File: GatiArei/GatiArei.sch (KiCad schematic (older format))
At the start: 38 parts

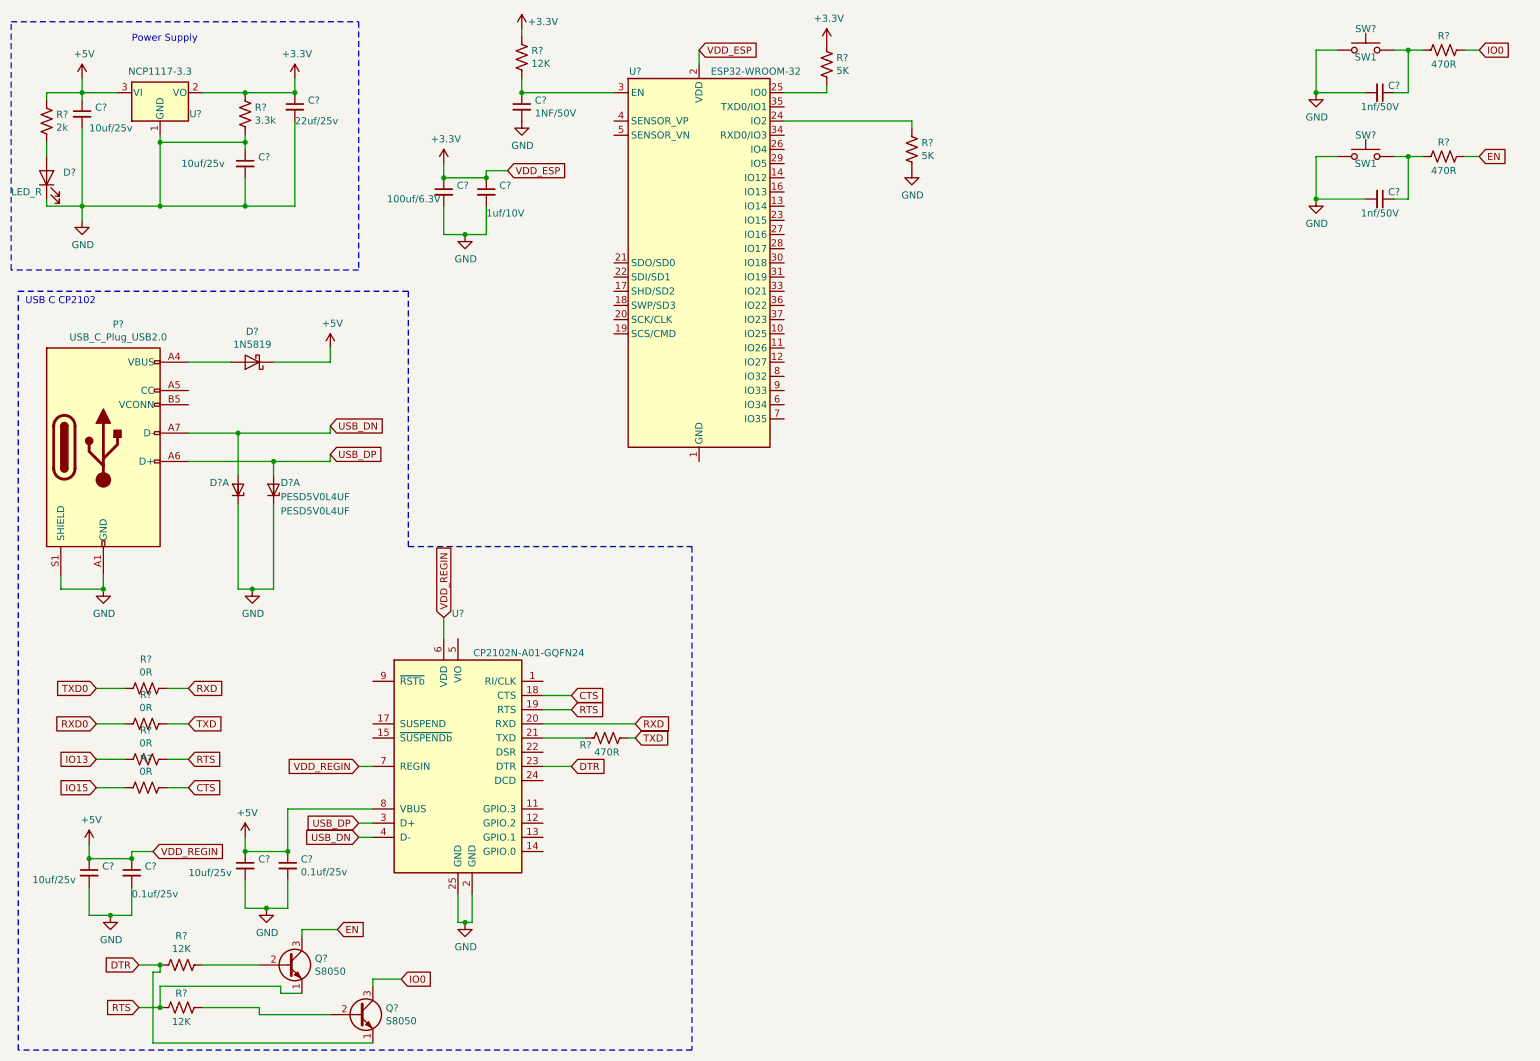
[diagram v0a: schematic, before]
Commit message: Adding the RFID and LCD port
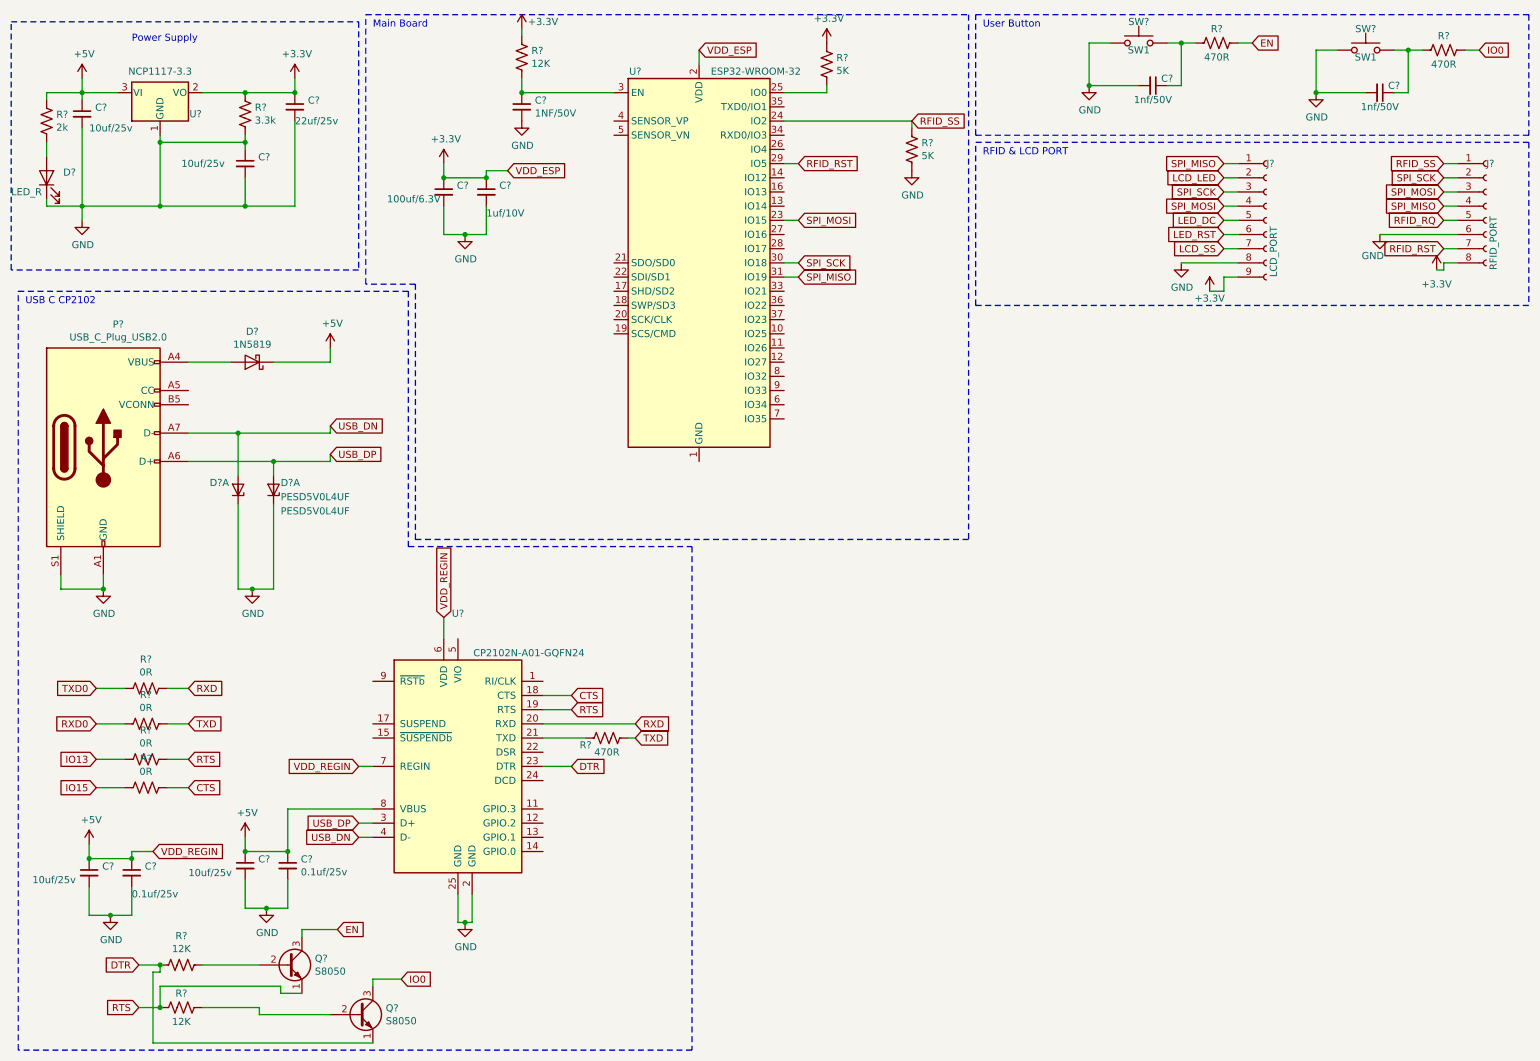
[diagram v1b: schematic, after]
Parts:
- added J?: RFID_PORT, symbol Connector:Conn_01x08_Female
- added J?: LCD_PORT, symbol Connector:Conn_01x09_Female
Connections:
- net +3V3: now also J?.8 (Pin_8), J?.9 (Pin_9)
- net GND: now also J?.6 (Pin_6), J?.8 (Pin_8)
- net SPI_MOSI: now reaches U?.23 (IO15)
- net SPI_MOSI: now also J?.3 (Pin_3), J?.4 (Pin_4)
- net RFID_SS: now reaches R?.1, U?.24 (IO2)
- net RFID_SS: now also J?.1 (Pin_1)
- net RFID_RST: now reaches U?.29 (IO5)
- net RFID_RST: now also J?.7 (Pin_7)
- net SPI_SCK: now reaches U?.30 (IO18)
- net SPI_SCK: now also J?.2 (Pin_2), J?.3 (Pin_3)
- net SPI_MISO: now reaches U?.31 (IO19)
- net SPI_MISO: now also J?.1 (Pin_1), J?.4 (Pin_4)
- new net LCD_LED: J?.2 (Pin_2)
- new net LCD_SS: J?.7 (Pin_7)
- new net LED_DC: J?.5 (Pin_5)
- new net LED_RST: J?.6 (Pin_6)
- new net RFID_RQ: J?.5 (Pin_5)
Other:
- note added: "Main Board"
- note added: "RFID & LCD PORT"
- note added: "User Button"
- moved on the sheet: C?, R?, SW?

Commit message: Adding Display Port
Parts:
- removed U?: NCP1117-3.3, Package_TO_SOT_SMD:SOT-223-3_TabPin2, symbol Regulator_Linear:NCP1117-3.3_SOT223
- added U1: MCP1700-3302E_SOT23, Package_TO_SOT_SMD:SOT-23, symbol Regulator_Linear:MCP1700-3302E_SOT23
- C1, C2, C4, C5: renamed from C?; footprint (none) -> Capacitor_SMD:C_1210_3225Metric
- C10, C11, C12, C3, C6, C7, C9: renamed from C?; footprint (none) -> Capacitor_SMD:C_0805_2012Metric
- C8: renamed from C?; footprint (none) -> Capacitor_Tantalum_SMD:CP_EIA-6032-15_Kemet-U
- D1: renamed from D?; footprint (none) -> LED_SMD:LED_0805_2012Metric
- J1: renamed from J?; footprint (none) -> Connector_PinHeader_2.54mm:PinHeader_1x09_P2.54mm_Vertical
- J2: renamed from J?; footprint (none) -> Connector_PinHeader_2.54mm:PinHeader_1x08_P2.54mm_Vertical
- P1: renamed from P?; footprint (none) -> Connector_USB:USB_C_Plug_Molex_105444
- R1, R10, R11, R12, R13, R14, R2, R3, R4, R5, R6, R7, R8, R9: renamed from R?; footprint (none) -> Resistor_SMD:R_0805_2012Metric
- SW1, SW2: renamed from SW?; footprint (none) -> Button_Switch_SMD:SW_DIP_SPSTx01_Slide_6.7x4.1mm_W6.73mm_P2.54mm_LowProfile_JPin
- gave numbers to parts that had none: 7
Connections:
- net LCD_LED is gone; now on net +3V3: J1.2 (Pin_2)
- net LED_DC is gone; now on net LCD_DC: J1.5 (Pin_5)
- net LED_RST is gone; now on net LCD_RST: J1.6 (Pin_6)
- net +3V3: now also U1.2 (VO)
- net +5V: now also U1.3 (VI)
- net GND: now also U1.1 (GND)
- net LCD_SS: now also U3.23 (IO15)
- net SPI_MOSI: now also U3.37 (IO23); no longer U3.23 (IO15)
- net LCD_DC: now reaches U3.16 (IO13)
- net LCD_RST: now reaches U3.26 (IO4)

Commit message: Adding PCB design
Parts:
- added J3: Bat_Con, Connector_PinHeader_2.00mm:PinHeader_1x02_P2.00mm_Vertical, symbol Connector:Conn_01x02_Female
- D2, D4: value PESD5V0L4UF -> ESD5V; footprint Package_TO_SOT_SMD:SOT-886 -> Package_TO_SOT_SMD:SOT-23
- D3: footprint Diode_THT:D_DO-41_SOD81_P10.16mm_Horizontal -> Diode_SMD:D_SMA
- P1: value USB_C_Plug_USB2.0 -> USB_C
- Q1, Q2: footprint Package_TO_SOT_THT:TO-92_Inline -> Package_TO_SOT_SMD:SOT-23
- U1: value MCP1700-3302E_SOT23 -> MCP1700
- U2: value CP2102N-A01-GQFN24 -> CP2102N
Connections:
- net +5V: now also J3.1 (Pin_1)
- net EN: now also C10.1, R9.2, U3.3 (EN)
- net GND: now also J3.2 (Pin_2)
- net IO0: now also R11.2, U3.25 (IO0)
- net RXD0: now also U3.34 (RXD0/IO3)
- net TXD0: now also U3.35 (TXD0/IO1)
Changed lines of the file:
@@
 P 3650 5800
 F 0 "U2" H 3650 6878 50  0000 C CNN
-F 1 "CP2102N-A01-GQFN24" H 4150 6600 50  0000 C CNN
+F 1 "CP2102N" H 4150 6600 50  0000 C CNN
 F 2 "Package_DFN_QFN:QFN-24-1EP_4x4mm_P0.5mm_EP2.6x2.6mm" H 4100 5000 50  0001 L CNN
 F 3 "http://www.silabs.com/support%20documents/technicaldocs/cp2102n-datasheet.pdf" H 3700 4750 50  0001 C CNN
@@
 P 1150 3550
 F 0 "P1" H 1255 4417 50  0000 C CNN
-F 1 "USB_C_Plug_USB2.0" H 1255 4326 50  0000 C CNN
+F 1 "USB_C" H 1255 4326 50  0000 C CNN
 F 2 "Connector_USB:USB_C_Plug_Molex_105444" H 1300 3550 50  0001 C CNN
 F 3 "https://www.usb.org/sites/default/files/documents/usb_type-c.zip" H 1300 3550 50  0001 C CNN
@@
 F 0 "D3" H 2200 2734 50  0000 C CNN
 F 1 "1N5819" H 2200 2825 50  0000 C CNN
-F 2 "Diode_THT:D_DO-41_SOD81_P10.16mm_Horizontal" H 2200 2775 50  0001 C CNN
+F 2 "Diode_SMD:D_SMA" H 2200 2775 50  0001 C CNN
 F 3 "http://www.vishay.com/docs/88525/1n5817.pdf" H 2200 2950 50  0001 C CNN
 	1    2200 2950
@@
 P 2100 3850
 F 0 "D2" V 2150 4050 50  0000 R CNN
-F 1 "PESD5V0L4UF" V 1950 3550 50  0000 R CNN
-F 2 "Package_TO_SOT_SMD:SOT-886" H 2100 3850 50  0001 C CNN
+F 1 "ESD5V" V 1950 3550 50  0000 R CNN
+F 2 "Package_TO_SOT_SMD:SOT-23" H 2100 3850 50  0001 C CNN
 F 3 "http://www.nxp.com/documents/data_sheet/PESDXL4UF_G_W.pdf" H 2100 3850 50  0001 C CNN
 	1    2100 3850
@@
 P 2350 3850
 F 0 "D4" V 2400 3800 50  0000 R CNN
-F 1 "PESD5V0L4UF" V 2300 3800 50  0000 R CNN
-F 2 "Package_TO_SOT_SMD:SOT-886" H 2350 3850 50  0001 C CNN
+F 1 "ESD5V" V 2300 3800 50  0000 R CNN
+F 2 "Package_TO_SOT_SMD:SOT-23" H 2350 3850 50  0001 C CNN
 F 3 "http://www.nxp.com/documents/data_sheet/PESDXL4UF_G_W.pdf" H 2350 3850 50  0001 C CNN
 	1    2350 3850
@@
 F 0 "Q1" H 2641 7246 50  0000 L CNN
 F 1 "S8050" H 2641 7155 50  0000 L CNN
-F 2 "Package_TO_SOT_THT:TO-92_Inline" H 2650 7125 50  0001 L CIN
+F 2 "Package_TO_SOT_SMD:SOT-23" H 2650 7125 50  0001 L CIN
 F 3 "http://www.unisonic.com.tw/datasheet/S8050.pdf" H 2450 7200 50  0001 L CNN
 	1    2450 7200
@@
 F 0 "Q2" H 3141 7596 50  0000 L CNN
 F 1 "S8050" H 3141 7505 50  0000 L CNN
-F 2 "Package_TO_SOT_THT:TO-92_Inline" H 3150 7475 50  0001 L CIN
+F 2 "Package_TO_SOT_SMD:SOT-23" H 3150 7475 50  0001 L CIN
 F 3 "http://www.unisonic.com.tw/datasheet/S8050.pdf" H 2950 7550 50  0001 L CNN
 	1    2950 7550
@@
 P 1550 1050
 F 0 "U1" H 1550 1292 50  0000 C CNN
-F 1 "MCP1700-3302E_SOT23" H 1550 1201 50  0000 C CNN
+F 1 "MCP1700" H 1550 1201 50  0000 C CNN
 F 2 "Package_TO_SOT_SMD:SOT-23" H 1550 1275 50  0001 C CNN
 F 3 "http://ww1.microchip.com/downloads/en/DeviceDoc/20001826C.pdf" H 1550 1050 50  0001 C CNN
@@
 	1    0    0    -1
 $EndComp
+$Comp
+L Connector:Conn_01x02_Female J3
+U 1 1 602F9AA9
+P 2050 2100
+F 0 "J3" H 2077 2076 50  0000 L CNN
+F 1 "Bat_Con" H 2077 1985 50  0000 L CNN
+F 2 "Connector_PinHeader_2.00mm:PinHeader_1x02_P2.00mm_Vertical" H 2050 2100 50  0001 C CNN
+F 3 "~" H 2050 2100 50  0001 C CNN
+	1    2050 2100
+	1    0    0    -1
+$EndComp
+Wire Wire Line
+	1850 2100 1700 2100
+Wire Wire Line
+	1850 2200 1700 2200
+Wire Wire Line
+	1700 2100 1700 2050
+$Comp
+L power:+5V #PWR025
+U 1 1 6030CD88
+P 1700 2050
+F 0 "#PWR025" H 1700 1900 50  0001 C CNN
+F 1 "+5V" H 1800 2150 50  0000 C CNN
+F 2 "" H 1700 2050 50  0001 C CNN
+F 3 "" H 1700 2050 50  0001 C CNN
+	1    1700 2050
+	1    0    0    -1
+$EndComp
+$Comp
+L power:GND #PWR026
+U 1 1 6030CEE9
+P 1700 2200
+F 0 "#PWR026" H 1700 1950 50  0001 C CNN
+F 1 "GND" H 1600 2200 50  0000 C CNN
+F 2 "" H 1700 2200 50  0001 C CNN
+F 3 "" H 1700 2200 50  0001 C CNN
+	1    1700 2200
+	1    0    0    -1
+$EndComp
+Wire Wire Line
+	5950 1150 6100 1150
+Wire Wire Line
+	5950 1350 6100 1350
+Text GLabel 6100 1150 2    50   Input ~ 0
+TXD0
+Text GLabel 6100 1350 2    50   Input ~ 0
+RXD0
+Text GLabel 4100 1050 0    50   Input ~ 0
+EN
+Text GLabel 6250 1050 2    50   Input ~ 0
+IO0
 $EndSCHEMATC
